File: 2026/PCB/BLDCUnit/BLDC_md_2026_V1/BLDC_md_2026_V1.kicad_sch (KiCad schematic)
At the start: 67 parts, among them J1 Conn_01x07_Pin, J2 Conn_01x02_Pin, J3 Conn_01x03_Socket, J4 Conn_01x02_Socket, SW1 SW_MEC_5E, SW2 SW_MEC_5E, U1 MAX3051

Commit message: フットプリント割当完了
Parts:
- C1, C10, C11, C12, C2, C3, C4, C5, C6, C7, C8, C9: footprint (none) -> Capacitor_SMD:C_0603_1608Metric_Pad1.08x0.95mm_HandSolder
- D1, D7: footprint (none) -> Diode_SMD:D_SMB
- D2: footprint (none) -> LED_SMD:LED_RGB_Wuerth-PLCC4_3.2x2.8mm_150141M173100
- D3, D4, D5, D6: footprint (none) -> BLDCUint_LIB_FTP:LED_1608_user_dif
- FET1, FET2, FET3: footprint (none) -> BLDCUint_LIB_FTP:SQJQ910EL-T1_GE3
- J1: footprint (none) -> Connector_JST:JST_PH_S7B-PH-K_1x07_P2.00mm_Horizontal
- J2: footprint (none) -> Connector_Molex:Molex_SPOX_5268-02A_1x02_P2.50mm_Horizontal
- J3: footprint (none) -> Connector_Molex:Molex_SPOX_5268-03A_1x03_P2.50mm_Horizontal
- J4: footprint (none) -> Connector_JST:JST_PH_S2B-PH-K_1x02_P2.00mm_Horizontal
- JP1, JP2: footprint (none) -> Jumper:SolderJumper-2_P1.3mm_Open_TrianglePad1.0x1.5mm
- L1: footprint (none) -> Inductor_SMD:L_Cenker_CKCS6020
- MCU1: footprint (none) -> Package_DFN_QFN:VQFN-64-1EP_9x9mm_P0.5mm_EP5.4x5.4mm
- R1, R2, R5, R6, R7: footprint (none) -> Resistor_SMD:R_0402_1005Metric_Pad0.72x0.64mm_HandSolder
- R3, R4: footprint (none) -> Resistor_SMD:R_0603_1608Metric_Pad0.98x0.95mm_HandSolder
- SENSE1: footprint (none) -> Package_SO:TSSOP-14_4.4x5mm_P0.65mm
- SW1, SW2: footprint (none) -> BLDCUint_LIB_FTP:SW_SKRPACE010
- U1: footprint (none) -> Package_SO:SOIC-8_3.9x4.9mm_P1.27mm
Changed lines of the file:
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@@
 			)
 		)
-		(property "Footprint" ""
+		(property "Footprint" "Diode_SMD:D_SMB"
 			(at 114.3 86.36 0)
 			(effects
@@
 			)
 		)
-		(property "Footprint" ""
+		(property "Footprint" "Connector_JST:JST_PH_S2B-PH-K_1x02_P2.00mm_Horizontal"
 			(at 260.35 133.35 0)
 			(effects
@@
 			)
 		)
-		(property "Footprint" ""
+		(property "Footprint" "BLDCUint_LIB_FTP:SQJQ910EL-T1_GE3"
 			(at 185.42 77.47 0)
 			(effects
@@
 			)
 		)
-		(property "Footprint" ""
+		(property "Footprint" "Jumper:SolderJumper-2_P1.3mm_Open_TrianglePad1.0x1.5mm"
 			(at 58.42 80.01 0)
 			(effects
@@
 			)
 		)
-		(property "Footprint" ""
+		(property "Footprint" "Capacitor_SMD:C_0603_1608Metric_Pad1.08x0.95mm_HandSolder"
 			(at 33.9852 39.37 0)
 			(effects
@@
 			)
 		)
-		(property "Footprint" ""
+		(property "Footprint" "Capacitor_SMD:C_0603_1608Metric_Pad1.08x0.95mm_HandSolder"
 			(at 74.93 172.4152 0)
 			(effects
@@
 			)
 		)
-		(property "Footprint" ""
+		(property "Footprint" "BLDCUint_LIB_FTP:LED_1608_user_dif"
 			(at 134.62 157.48 0)
 			(effects
@@
 			)
 		)
-		(property "Footprint" ""
+		(property "Footprint" "Capacitor_SMD:C_0603_1608Metric_Pad1.08x0.95mm_HandSolder"
 			(at 28.9052 39.37 0)
 			(effects
@@
 			)
 		)
-		(property "Footprint" ""
+		(property "Footprint" "Inductor_SMD:L_Cenker_CKCS6020"
 			(at 120.65 80.01 0)
 			(effects
@@
 			)
 		)
-		(property "Description" "Inductor"
+		(property "Description" "SDE0604A-180M"
 			(at 120.65 80.01 0)
 			(effects
@@
 			)
 		)
-		(property "Footprint" ""
+		(property "Footprint" "BLDCUint_LIB_FTP:LED_1608_user_dif"
 			(at 134.62 152.4 0)
 			(effects
@@
 			)
 		)
-		(property "Footprint" ""
+		(property "Footprint" "Package_SO:TSSOP-14_4.4x5mm_P0.65mm"
 			(at 175.26 132.08 0)
 			(effects
@@
 			)
 		)
-		(property "Footprint" ""
+		(property "Footprint" "Package_SO:SOIC-8_3.9x4.9mm_P1.27mm"
 			(at 229.87 132.08 0)
 			(effects
@@
 			)
 		)
-		(property "Footprint" ""
+		(property "Footprint" "Capacitor_SMD:C_0603_1608Metric_Pad1.08x0.95mm_HandSolder"
 			(at 36.83 172.4152 0)
 			(effects
@@
 			)
 		)
-		(property "Footprint" ""
+		(property "Footprint" "Connector_Molex:Molex_SPOX_5268-03A_1x03_P2.50mm_Horizontal"
 			(at 213.36 97.79 0)
 			(effects
@@
 			)
 		)
-		(property "Footprint" ""
+		(property "Footprint" "Connector_JST:JST_PH_S7B-PH-K_1x07_P2.00mm_Horizontal"
 			(at 40.64 113.03 0)
 			(effects
@@
 			)
 		)
-		(property "Footprint" ""
+		(property "Footprint" "Capacitor_SMD:C_0603_1608Metric_Pad1.08x0.95mm_HandSolder"
 			(at 49.2252 39.37 0)
 			(effects
@@
 			)
 		)
-		(property "Footprint" ""
+		(property "Footprint" "BLDCUint_LIB_FTP:LED_1608_user_dif"
 			(at 134.62 162.56 0)
 			(effects
@@
 			)
 		)
-		(property "Footprint" ""
+		(property "Footprint" "Capacitor_SMD:C_0603_1608Metric_Pad1.08x0.95mm_HandSolder"
 			(at 23.8252 39.37 0)
 			(effects
@@
 			)
 		)
-		(property "Footprint" ""
+		(property "Footprint" "Jumper:SolderJumper-2_P1.3mm_Open_TrianglePad1.0x1.5mm"
 			(at 58.42 77.47 0)
 			(effects
@@
 			)
 		)
-		(property "Footprint" ""
+		(property "Footprint" "BLDCUint_LIB_FTP:SQJQ910EL-T1_GE3"
 			(at 185.42 57.15 0)
 			(effects
@@
 			)
 		)
-		(property "Footprint" ""
+		(property "Footprint" "Resistor_SMD:R_0603_1608Metric_Pad0.98x0.95mm_HandSolder"
 			(at 50.292 157.48 90)
 			(effects
@@
 			)
 		)
-		(property "Footprint" ""
+		(property "Footprint" "BLDCUint_LIB_FTP:SQJQ910EL-T1_GE3"
 			(at 185.42 36.83 0)
 			(effects
@@
 			)
 		)
-		(property "Footprint" ""
+		(property "Footprint" "Resistor_SMD:R_0603_1608Metric_Pad0.98x0.95mm_HandSolder"
 			(at 88.392 157.48 90)
 			(effects
@@
 			)
 		)
-		(property "Footprint" ""
+		(property "Footprint" "Resistor_SMD:R_0402_1005Metric_Pad0.72x0.64mm_HandSolder"
 			(at 43.942 78.74 90)
 			(effects
@@
 			)
 		)
-		(property "Footprint" ""
+		(property "Footprint" "LED_SMD:LED_RGB_Wuerth-PLCC4_3.2x2.8mm_150141M173100"
 			(at 124.46 104.14 0)
 			(effects
@@
 			)
 		)
-		(property "Description" "RGB LED, blue/red/green/cathode"
+		(property "Description" "XZM2CRKM2DGFBB45SCCB"
 			(at 124.46 105.41 0)
 			(effects
@@
 			)
 		)
-		(property "Footprint" ""
+		(property "Footprint" "Capacitor_SMD:C_0603_1608Metric_Pad1.08x0.95mm_HandSolder"
 			(at 127.9652 90.17 0)
 			(effects
@@
 			)
 		)
-		(property "Footprint" ""
+		(property "Footprint" "Resistor_SMD:R_0402_1005Metric_Pad0.72x0.64mm_HandSolder"
 			(at 110.49 107.188 90)
 			(effects
@@
 			)
 		)
-		(property "Footprint" ""
+		(property "Footprint" "Resistor_SMD:R_0402_1005Metric_Pad0.72x0.64mm_HandSolder"
 			(at 43.942 66.04 90)
 			(effects
@@
 			)
 		)
-		(property "Footprint" ""
+		(property "Footprint" "Resistor_SMD:R_0402_1005Metric_Pad0.72x0.64mm_HandSolder"
 			(at 110.49 104.648 90)
 			(effects
@@
 			)
 		)
-		(property "Footprint" ""
+		(property "Footprint" "Capacitor_SMD:C_0603_1608Metric_Pad1.08x0.95mm_HandSolder"
 			(at 39.0652 39.37 0)
 			(effects
@@
 			)
 		)
-		(property "Footprint" ""
+		(property "Footprint" "BLDCUint_LIB_FTP:SW_SKRPACE010"
 			(at 78.74 158.75 0)
 			(effects
@@
 			)
 		)
-		(property "Footprint" ""
+		(property "Footprint" "Diode_SMD:D_SMB"
 			(at 198.12 91.44 0)
 			(effects
@@
 			)
 		)
-		(property "Footprint" ""
+		(property "Footprint" "BLDCUint_LIB_FTP:LED_1608_user_dif"
 			(at 134.62 147.32 0)
 			(effects
@@
 			)
 		)
-		(property "Footprint" ""
+		(property "Footprint" "Connector_Molex:Molex_SPOX_5268-02A_1x02_P2.50mm_Horizontal"
 			(at 121.92 179.07 0)
 			(effects
@@
 			)
 		)
-		(property "Footprint" ""
+		(property "Footprint" "Capacitor_SMD:C_0603_1608Metric_Pad1.08x0.95mm_HandSolder"
 			(at 39.0652 54.61 0)
 			(effects
@@
 			)
 		)
-		(property "Footprint" ""
+		(property "Footprint" "Capacitor_SMD:C_0603_1608Metric_Pad1.08x0.95mm_HandSolder"
 			(at 41.6052 82.55 0)
 			(effects
@@
 			)
 		)
-		(property "Footprint" ""
+		(property "Footprint" "Package_DFN_QFN:VQFN-64-1EP_9x9mm_P0.5mm_EP5.4x5.4mm"
 			(at 85.09 72.39 0)
 			(effects
@@
 			)
 		)
-		(property "Footprint" ""
+		(property "Footprint" "Capacitor_SMD:C_0603_1608Metric_Pad1.08x0.95mm_HandSolder"
 			(at 44.1452 39.37 0)
 			(effects
@@
 			)
 		)
-		(property "Footprint" ""
+		(property "Footprint" "Capacitor_SMD:C_0603_1608Metric_Pad1.08x0.95mm_HandSolder"
 			(at 133.0452 90.17 0)
 			(effects
@@
 			)
 		)
-		(property "Footprint" ""
+		(property "Footprint" "BLDCUint_LIB_FTP:SW_SKRPACE010"
 			(at 40.64 158.75 0)
 			(effects
@@
 			)
 		)
-		(property "Footprint" ""
+		(property "Footprint" "Resistor_SMD:R_0402_1005Metric_Pad0.72x0.64mm_HandSolder"
 			(at 110.49 109.728 90)
 			(effects

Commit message: PCBレイアウト開始
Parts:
- removed C19: 10u, Capacitor_SMD:C_1210_3225Metric_Pad1.33x2.70mm_HandSolder, symbol Device:C
- removed SENSE1: AS5048A-HTSP-500, Package_SO:TSSOP-14_4.4x5mm_P0.65mm, symbol BLDCUnit_LIB_SYM:AS5048A-HTSP-500
- added J5: Conn_01x06_Socket, Connector_JST:JST_PH_S6B-PH-K_1x06_P2.00mm_Horizontal, symbol Connector:Conn_01x06_Socket
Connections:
- net +3V3: now also J5.1 (Pin_1)
- net GND: now also J5.2 (Pin_2)
- net SPI1_CS: now also J5.3 (Pin_3)
- net SPI1_MISO: now also J5.5 (Pin_5)
- net SPI1_MOSI: now also J5.6 (Pin_6)
- net SPI1_SCK: now also J5.4 (Pin_4)
- no-connect marks 2 -> 0

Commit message: U,V,W生やした
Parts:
- D1: footprint Diode_SMD:D_SMB -> BLDCUint_LIB_FTP:MA10EB045
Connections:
- net BLDC_U: now also C24.1, FET3.2 (S1), FET3.5 (D2), J3.3 (Pin_3)
- net BLDC_V: now also C23.1, FET2.2 (S1), FET2.5 (D2), J3.2 (Pin_2)
- net BLDC_W: now also C22.1, FET1.2 (S1), FET1.5 (D2), J3.1 (Pin_1)
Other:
- moved on the sheet: J3
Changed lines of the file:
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@@
 	)
 	(junction
-		(at 203.2 59.69)
-		(diameter 0)
-		(color 0 0 0 0)
-	)
-	(junction
 		(at 50.8 80.01)
 		(diameter 0)
@@
 	)
 	(junction
-		(at 43.18 41.91)
+		(at 205.74 90.17)
 		(diameter 0)
 		(color 0 0 0 0)
 	)
 	(junction
-		(at 140.97 157.48)
+		(at 43.18 41.91)
 		(diameter 0)
 		(color 0 0 0 0)
 	)
 	(junction
-		(at 189.23 95.25)
+		(at 140.97 157.48)
 		(diameter 0)
 		(color 0 0 0 0)
 	)
 	(junction
-		(at 189.23 87.63)
+		(at 189.23 95.25)
 		(diameter 0)
 		(color 0 0 0 0)
 	)
 	(junction
-		(at 205.74 39.37)
+		(at 189.23 87.63)
 		(diameter 0)
 		(color 0 0 0 0)
@@
 	)
 	(junction
+		(at 200.66 80.01)
+		(diameter 0)
+		(color 0 0 0 0)
+	)
+	(junction
 		(at 205.74 34.29)
 		(diameter 0)
@@
 	)
 	(junction
+		(at 200.66 95.25)
+		(diameter 0)
+		(color 0 0 0 0)
+	)
+	(junction
 		(at 184.15 87.63)
 		(diameter 0)
@@
 	)
 	(junction
+		(at 203.2 92.71)
+		(diameter 0)
+		(color 0 0 0 0)
+	)
+	(junction
 		(at 40.64 85.09)
 		(diameter 0)
@@
 	)
 	(junction
-		(at 200.66 80.01)
-		(diameter 0)
-		(color 0 0 0 0)
-	)
-	(junction
 		(at 229.87 144.78)
 		(diameter 0)
@@
 	)
 	(junction
+		(at 203.2 59.69)
+		(diameter 0)
+		(color 0 0 0 0)
+	)
+	(junction
 		(at 52.07 166.37)
 		(diameter 0)
@@
 	)
 	(junction
+		(at 205.74 39.37)
+		(diameter 0)
+		(color 0 0 0 0)
+	)
+	(junction
 		(at 63.5 24.13)
 		(diameter 0)
@@
 	(wire
 		(pts
-			(xy 200.66 100.33) (xy 208.28 100.33)
+			(xy 200.66 95.25) (xy 208.28 95.25)
 		)
 		(stroke
@@
 	(wire
 		(pts
+			(xy 200.66 80.01) (xy 200.66 95.25)
+		)
+		(stroke
+			(width 0)
+			(type default)
+		)
+	)
+	(wire
+		(pts
 			(xy 104.14 59.69) (xy 106.68 59.69)
 		)
@@
 	(wire
 		(pts
-			(xy 200.66 80.01) (xy 200.66 100.33)
-		)
-		(stroke
-			(width 0)
-			(type default)
-		)
-	)
-	(wire
-		(pts
 			(xy 198.12 31.75) (xy 198.12 52.07)
 		)
@@
 	(wire
 		(pts
-			(xy 203.2 97.79) (xy 208.28 97.79)
+			(xy 203.2 92.71) (xy 208.28 92.71)
 		)
 		(stroke
@@
 	(wire
 		(pts
+			(xy 203.2 92.71) (xy 203.2 97.79)
+		)
+		(stroke
+			(width 0)
+			(type default)
+		)
+	)
+	(wire
+		(pts
 			(xy 63.5 29.21) (xy 63.5 31.75)
 		)
@@
 	(wire
 		(pts
+			(xy 205.74 39.37) (xy 205.74 90.17)
+		)
+		(stroke
+			(width 0)
+			(type default)
+		)
+	)
+	(wire
+		(pts
 			(xy 106.68 113.03) (xy 106.68 115.57)
 		)
@@
 	(wire
 		(pts
-			(xy 205.74 39.37) (xy 205.74 95.25)
-		)
-		(stroke
-			(width 0)
-			(type default)
-		)
-	)
-	(wire
-		(pts
 			(xy 33.02 41.91) (xy 38.1 41.91)
 		)
@@
 	(wire
 		(pts
-			(xy 205.74 95.25) (xy 208.28 95.25)
+			(xy 205.74 90.17) (xy 208.28 90.17)
 		)
 		(stroke
@@
 	(wire
 		(pts
+			(xy 200.66 95.25) (xy 200.66 97.79)
+		)
+		(stroke
+			(width 0)
+			(type default)
+		)
+	)
+	(wire
+		(pts
 			(xy 255.27 133.35) (xy 252.73 133.35)
 		)
@@
 	(wire
 		(pts
+			(xy 205.74 90.17) (xy 205.74 97.79)
+		)
+		(stroke
+			(width 0)
+			(type default)
+		)
+	)
+	(wire
+		(pts
 			(xy 140.97 147.32) (xy 140.97 152.4)
 		)
@@
 	(wire
 		(pts
-			(xy 203.2 59.69) (xy 203.2 97.79)
-		)
-		(stroke
-			(width 0)
-			(type default)
-		)
-	)
-	(wire
-		(pts
 			(xy 198.12 52.07) (xy 198.12 72.39)
 		)
@@
 	(wire
 		(pts
+			(xy 203.2 59.69) (xy 203.2 92.71)
+		)
+		(stroke
+			(width 0)
+			(type default)
+		)
+	)
+	(wire
+		(pts
 			(xy 104.14 115.57) (xy 106.68 115.57)
 		)
@@
 		)
 	)
+	(global_label "BLDC_U"
+		(shape input)
+		(at 200.66 97.79 270)
+		(fields_autoplaced yes)
+		(effects
+			(font
+				(size 1.27 1.27)
+			)
+			(justify right)
+		)
+		(property "Intersheetrefs" "${INTERSHEET_REFS}"
+			(at 200.66 107.9114 90)
+			(effects
+				(font
+					(size 1.27 1.27)
+				)
+				(justify right)
+				(hide yes)
+			)
+		)
+	)
 	(global_label "OP1_VINM"
 		(shape input)
@@
 		)
 	)
+	(global_label "BLDC_W"
+		(shape input)
+		(at 205.74 97.79 270)
+		(fields_autoplaced yes)
+		(effects
+			(font
+				(size 1.27 1.27)
+			)
+			(justify right)
+		)
+		(property "Intersheetrefs" "${INTERSHEET_REFS}"
+			(at 205.74 108.0323 90)
+			(effects
+				(font
+					(size 1.27 1.27)
+				)
+				(justify right)
+				(hide yes)
+			)
+		)
+	)
 	(global_label "USW"
 		(shape output)
@@
 		)
 	)
+	(global_label "BLDC_V"
+		(shape input)
+		(at 203.2 97.79 270)
+		(fields_autoplaced yes)
+		(effects
+			(font
+				(size 1.27 1.27)
+			)
+			(justify right)
+		)
+		(property "Intersheetrefs" "${INTERSHEET_REFS}"
+			(at 203.2 107.6695 90)
+			(effects
+				(font
+					(size 1.27 1.27)
+				)
+				(justify right)
+				(hide yes)
+			)
+		)
+	)
 	(global_label "USART_RX"
 		(shape input)
@@
 			)
 		)
-		(property "Footprint" "Diode_SMD:D_SMB"
+		(property "Footprint" "BLDCUint_LIB_FTP:MA10EB045"
 			(at 114.3 86.36 0)
 			(effects
@@
 			)
 		)
-		(property "Description" "Diode"
+		(property "Description" "MA10EB045"
 			(at 114.3 86.36 0)
 			(effects
@@
 					(size 1.27 1.27)
 				)
-				(hide yes)
 			)
 		)
@@
 		(on_board yes)
 		(dnp no)
-		(fields_autoplaced yes)
 		(property "Reference" "L1"
 			(at 120.65 74.93 90)
@@
 		)
 		(property "Description" "SDE0604A-180M"
-			(at 120.65 80.01 0)
+			(at 120.65 80.01 90)
 			(effects
 				(font
 					(size 1.27 1.27)
 				)
-				(hide yes)
 			)
 		)
@@
 	(symbol
 		(lib_id "Connector:Conn_01x03_Socket")
-		(at 213.36 97.79 0)
+		(at 213.36 92.71 0)
 		(unit 1)
 		(exclude_from_sim no)
@@
 		(dnp no)
 		(property "Reference" "J3"
-			(at 214.63 96.5199 0)
+			(at 214.63 91.4399 0)
 			(effects
 				(font
@@
 		)
 		(property "Value" "Conn_01x03_Socket"
-			(at 197.104 102.108 0)
+			(at 197.104 97.028 0)
 			(effects
 				(font
@@
 		)
 		(property "Footprint" "Connector_Molex:Molex_SPOX_5268-03A_1x03_P2.50mm_Horizontal"
-			(at 213.36 97.79 0)
+			(at 213.36 92.71 0)
 			(effects
 				(font
@@
 		)
 		(property "Datasheet" "~"
-			(at 213.36 97.79 0)
+			(at 213.36 92.71 0)
 			(effects
 				(font
@@
 		)
 		(property "Description" "Generic connector, single row, 01x03, script generated"
-			(at 213.36 97.79 0)
+			(at 213.36 92.71 0)
 			(effects
 				(font
@@
 					(size 1.27 1.27)
 				)
-				(hide yes)
 			)
 		)
@@
 			)
 		)
-		(property "Description" "Diode"
+		(property "Description" "SMBJ90CA"
 			(at 198.12 91.44 0)
 			(effects
@@
 					(size 1.27 1.27)
 				)
-				(hide yes)
 			)
 		)

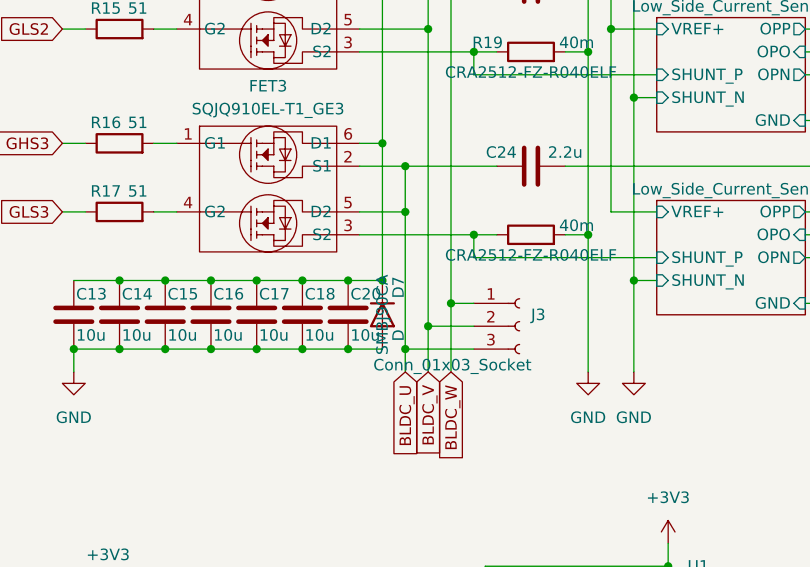
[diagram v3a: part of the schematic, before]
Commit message: 基板外形決定
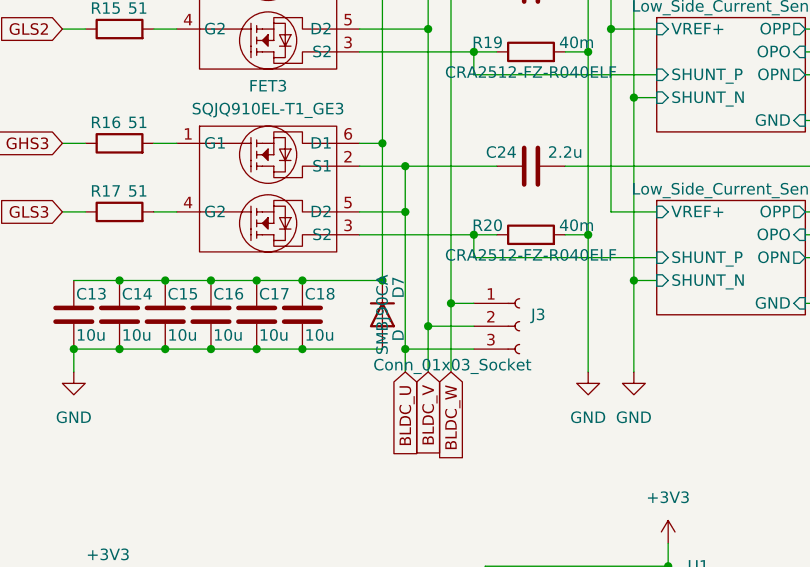
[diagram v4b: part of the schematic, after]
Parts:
- removed C20: 10u, Capacitor_SMD:C_1210_3225Metric_Pad1.33x2.70mm_HandSolder, symbol Device:C
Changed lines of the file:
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@@
 	)
 	(junction
-		(at 194.31 95.25)
-		(diameter 0)
-		(color 0 0 0 0)
-	)
-	(junction
-		(at 194.31 87.63)
-		(diameter 0)
-		(color 0 0 0 0)
-	)
-	(junction
 		(at 48.26 29.21)
 		(diameter 0)
@@
 	(wire
 		(pts
-			(xy 189.23 95.25) (xy 194.31 95.25)
-		)
-		(stroke
-			(width 0)
-			(type default)
-		)
-	)
-	(wire
-		(pts
 			(xy 229.87 144.78) (xy 229.87 147.32)
 		)
@@
 	(wire
 		(pts
-			(xy 194.31 95.25) (xy 198.12 95.25)
+			(xy 189.23 95.25) (xy 198.12 95.25)
 		)
 		(stroke
@@
 	(wire
 		(pts
-			(xy 194.31 87.63) (xy 198.12 87.63)
+			(xy 189.23 87.63) (xy 198.12 87.63)
 		)
 		(stroke
@@
 	(wire
 		(pts
-			(xy 189.23 87.63) (xy 194.31 87.63)
-		)
-		(stroke
-			(width 0)
-			(type default)
-		)
-	)
-	(wire
-		(pts
 			(xy 63.5 59.69) (xy 66.04 59.69)
 		)
@@
 					(size 1.27 1.27)
 				)
-				(hide yes)
 			)
 		)
@@
 					(unit 1)
 				)
-			)
-		)
-	)
-	(symbol
-		(lib_id "Device:C")
-		(at 194.31 91.44 0)
-		(unit 1)
-		(exclude_from_sim no)
-		(in_bom yes)
-		(on_board yes)
-		(dnp no)
-		(property "Reference" "C20"
-			(at 194.564 89.154 0)
-			(effects
-				(font
-					(size 1.27 1.27)
-				)
-				(justify left)
-			)
-		)
-		(property "Value" "10u"
-			(at 194.564 93.726 0)
-			(effects
-				(font
-					(size 1.27 1.27)
-				)
-				(justify left)
-			)
-		)
-		(property "Footprint" "Capacitor_SMD:C_1210_3225Metric_Pad1.33x2.70mm_HandSolder"
-			(at 195.2752 95.25 0)
-			(effects
-				(font
-					(size 1.27 1.27)
-				)
-				(hide yes)
-			)
-		)
-		(property "Datasheet" "~"
-			(at 194.31 91.44 0)
-			(effects
-				(font
-					(size 1.27 1.27)
-				)
-				(hide yes)
-			)
-		)
-		(property "Description" "GRM32EC72A106KE05L"
-			(at 194.31 91.44 0)
-			(effects
-				(font
-					(size 1.27 1.27)
-				)
-				(hide yes)
-			)
-		)
-		(pin "1"
-		)
-		(pin "2"
-		)
-		(instances
-			(project "BLDC_md_2026_V1"
-				(path "/b60d34e1-e978-4abb-befd-6af7b603dc53"
-					(reference "C20")
-					(unit 1)
-				)
